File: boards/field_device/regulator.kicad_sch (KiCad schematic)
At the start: 13 parts, among them U5 HX8001-AJC

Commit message: assigned better footprints
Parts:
- C10: footprint Capacitor_SMD:C_0201_0603Metric -> Capacitor_SMD:C_0805_2012Metric_Pad1.18x1.45mm_HandSolder
- C11, C13: footprint Sensor_Current:LEM_HX02-P -> Capacitor_SMD:C_0603_1608Metric_Pad1.08x0.95mm_HandSolder
- C12: footprint Sensor_Current:LEM_HX02-P -> Capacitor_SMD:C_0805_2012Metric_Pad1.18x1.45mm_HandSolder
- D4: footprint (none) -> LED_SMD:LED_0603_1608Metric_Pad1.05x0.95mm_HandSolder
- L1: footprint (none) -> UnEasy-LCSC:IND-SMD_L4.0-W4.0_B
- R15, R16, R19, R20: footprint (none) -> Capacitor_SMD:C_0603_1608Metric_Pad1.08x0.95mm_HandSolder
- R17, R18: footprint (none) -> Resistor_SMD:R_0402_1005Metric_Pad0.72x0.64mm_HandSolder
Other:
- moved on the sheet: C10
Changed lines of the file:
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@@
-	)
-	(junction
-		(at 22.86 57.15)
-		(diameter 0)
-		(color 0 0 0 0)
 	)
 	(junction
@@
 		(color 0 0 0 0)
 	)
+	(junction
+		(at 19.05 36.83)
+		(diameter 0)
+		(color 0 0 0 0)
+	)
 	(no_connect
 		(at 100.33 34.29)
@@
 	(wire
 		(pts
-			(xy 62.23 50.8) (xy 62.23 52.07)
+			(xy 19.05 36.83) (xy 22.86 36.83)
 		)
 		(stroke
@@
 	(wire
 		(pts
-			(xy 64.77 31.75) (xy 64.77 34.29)
+			(xy 62.23 50.8) (xy 62.23 52.07)
 		)
 		(stroke
@@
 	(wire
 		(pts
-			(xy 64.77 34.29) (xy 80.01 34.29)
+			(xy 64.77 31.75) (xy 64.77 34.29)
 		)
 		(stroke
@@
 	(wire
 		(pts
-			(xy 62.23 49.53) (xy 62.23 50.8)
+			(xy 64.77 34.29) (xy 80.01 34.29)
 		)
 		(stroke
@@
 	(wire
 		(pts
-			(xy 21.59 57.15) (xy 22.86 57.15)
+			(xy 62.23 49.53) (xy 62.23 50.8)
 		)
 		(stroke
@@
 	(wire
 		(pts
-			(xy 100.33 31.75) (xy 115.57 31.75)
+			(xy 17.78 36.83) (xy 19.05 36.83)
 		)
 		(stroke
@@
 	(wire
 		(pts
-			(xy 35.56 36.83) (xy 80.01 36.83)
+			(xy 100.33 31.75) (xy 115.57 31.75)
 		)
 		(stroke
@@
 	(wire
 		(pts
-			(xy 107.95 39.37) (xy 107.95 36.83)
+			(xy 35.56 36.83) (xy 80.01 36.83)
 		)
 		(stroke
@@
 	(wire
 		(pts
-			(xy 64.77 50.8) (xy 64.77 34.29)
+			(xy 107.95 39.37) (xy 107.95 36.83)
 		)
 		(stroke
@@
 	(wire
 		(pts
-			(xy 34.29 36.83) (xy 35.56 36.83)
+			(xy 64.77 50.8) (xy 64.77 34.29)
 		)
 		(stroke
@@
 	(wire
 		(pts
-			(xy 22.86 36.83) (xy 26.67 36.83)
+			(xy 34.29 36.83) (xy 35.56 36.83)
 		)
 		(stroke
@@
 	(wire
 		(pts
-			(xy 50.8 41.91) (xy 62.23 41.91)
+			(xy 22.86 36.83) (xy 26.67 36.83)
 		)
 		(stroke
@@
 	(wire
 		(pts
-			(xy 22.86 36.83) (xy 22.86 57.15)
+			(xy 50.8 41.91) (xy 62.23 41.91)
 		)
 		(stroke
@@
 	(hierarchical_label "Vin"
 		(shape input)
-		(at 21.59 57.15 180)
+		(at 17.78 36.83 180)
 		(effects
 			(font
@@
 			)
 		)
-		(property "Footprint" ""
+		(property "Footprint" "Capacitor_SMD:C_0603_1608Metric_Pad1.08x0.95mm_HandSolder"
 			(at 113.792 35.56 90)
 			(hide yes)
@@
 			)
 		)
-		(property "Footprint" ""
+		(property "Footprint" "Capacitor_SMD:C_0603_1608Metric_Pad1.08x0.95mm_HandSolder"
 			(at 30.48 38.608 90)
 			(hide yes)
@@
 			)
 		)
-		(property "Footprint" ""
+		(property "Footprint" "Capacitor_SMD:C_0603_1608Metric_Pad1.08x0.95mm_HandSolder"
 			(at 68.58 33.528 90)
 			(hide yes)
@@
 		(dnp no)
 		(fields_autoplaced yes)
-		(property "Reference" "#PWR026"
+		(property "Reference" "#PWR027"
 			(at 22.86 40.64 0)
 			(hide yes)
@@
 			(project "field_device"
 				(path "/99623870-118f-49fe-bbf0-fb0b890db442/e9c11804-cc5e-4b00-a5de-7502c32ebb51/ed5659f9-5584-4daa-a017-4d4def535a07"
-					(reference "#PWR026")
+					(reference "#PWR027")
 					(unit 1)
 				)
@@
 			)
 		)
-		(property "Footprint" ""
+		(property "Footprint" "Capacitor_SMD:C_0603_1608Metric_Pad1.08x0.95mm_HandSolder"
 			(at 52.578 45.72 90)
 			(hide yes)
@@
 			)
 		)
-		(property "Footprint" ""
+		(property "Footprint" "Resistor_SMD:R_0402_1005Metric_Pad0.72x0.64mm_HandSolder"
 			(at 64.008 55.88 90)
 			(hide yes)
@@
 			)
 		)
-		(property "Footprint" ""
+		(property "Footprint" "UnEasy-LCSC:IND-SMD_L4.0-W4.0_B"
 			(at 104.14 36.83 0)
 			(hide yes)
@@
 			)
 		)
-		(property "Footprint" ""
+		(property "Footprint" "LED_SMD:LED_0603_1608Metric_Pad1.05x0.95mm_HandSolder"
 			(at 50.8 53.34 0)
 			(hide yes)
@@
 			)
 		)
-		(property "Footprint" "Sensor_Current:LEM_HX02-P"
+		(property "Footprint" "Capacitor_SMD:C_0603_1608Metric_Pad1.08x0.95mm_HandSolder"
 			(at 80.01 30.7848 0)
 			(hide yes)
@@
 			)
 		)
-		(property "Footprint" "Sensor_Current:LEM_HX02-P"
+		(property "Footprint" "Capacitor_SMD:C_0805_2012Metric_Pad1.18x1.45mm_HandSolder"
 			(at 73.9648 49.53 0)
 			(hide yes)
@@
 			)
 		)
-		(property "Footprint" "Sensor_Current:LEM_HX02-P"
+		(property "Footprint" "Capacitor_SMD:C_0603_1608Metric_Pad1.08x0.95mm_HandSolder"
 			(at 34.5948 44.45 0)
 			(hide yes)
@@
 			)
 		)
-		(property "Footprint" ""
+		(property "Footprint" "Resistor_SMD:R_0402_1005Metric_Pad0.72x0.64mm_HandSolder"
 			(at 64.008 45.72 90)
 			(hide yes)
@@
 	(symbol
 		(lib_id "power:GND")
-		(at 22.86 64.77 0)
+		(at 19.05 44.45 0)
 		(unit 1)
 		(body_style 1)
@@
 		(dnp no)
 		(fields_autoplaced yes)
-		(property "Reference" "#PWR027"
-			(at 22.86 71.12 0)
+		(property "Reference" "#PWR026"
+			(at 19.05 50.8 0)
 			(hide yes)
 			(show_name no)
@@
 		)
 		(property "Value" "GND"
-			(at 22.86 69.85 0)
+			(at 19.05 49.53 0)
 			(show_name no)
 			(do_not_autoplace no)
@@
 		)
 		(property "Footprint" ""
-			(at 22.86 64.77 0)
-			(hide yes)
-			(show_name no)
-			(do_not_autoplace no)
-			(effects
-				(font
-					(size 1.27 1.27)
-				)
-			)
-		)
-		(property "Datasheet" ""
-			(at 22.86 64.77 0)
+			(at 19.05 44.45 0)
+			(hide yes)
+			(show_name no)
+			(do_not_autoplace no)
+			(effects
+				(font
+					(size 1.27 1.27)
+				)
+			)
+		)
+		(property "Datasheet" ""
+			(at 19.05 44.45 0)
 			(hide yes)
 			(show_name no)
@@
 		)
 		(property "Description" "Power symbol creates a global label with name \"GND\" , ground"
-			(at 22.86 64.77 0)
-			(hide yes)
-			(show_name no)
-			(do_not_autoplace no)
-			(effects
-				(font
-					(size 1.27 1.27)
-				)
-			)
-		)
-		(pin "1"
-		)
-		(instances
-			(project "field_device"
-				(path "/99623870-118f-49fe-bbf0-fb0b890db442/e9c11804-cc5e-4b00-a5de-7502c32ebb51/ed5659f9-5584-4daa-a017-4d4def535a07"
-					(reference "#PWR027")
+			(at 19.05 44.45 0)
+			(hide yes)
+			(show_name no)
+			(do_not_autoplace no)
+			(effects
+				(font
+					(size 1.27 1.27)
+				)
+			)
+		)
+		(pin "1"
+		)
+		(instances
+			(project "field_device"
+				(path "/99623870-118f-49fe-bbf0-fb0b890db442/e9c11804-cc5e-4b00-a5de-7502c32ebb51/ed5659f9-5584-4daa-a017-4d4def535a07"
+					(reference "#PWR026")
 					(unit 1)
 				)
@@
 	(symbol
 		(lib_id "Device:C")
-		(at 22.86 60.96 0)
+		(at 19.05 40.64 0)
 		(unit 1)
 		(body_style 1)
@@
 		(fields_autoplaced yes)
 		(property "Reference" "C10"
-			(at 26.67 59.6899 0)
+			(at 22.86 39.3699 0)
 			(show_name no)
 			(do_not_autoplace no)
@@
 		)
 		(property "Value" "10u"
-			(at 26.67 62.2299 0)
+			(at 22.86 41.9099 0)
 			(show_name no)
 			(do_not_autoplace no)
@@
 			)
 		)
-		(property "Footprint" "Capacitor_SMD:C_0201_0603Metric"
-			(at 23.8252 64.77 0)
-			(hide yes)
-			(show_name no)
-			(do_not_autoplace no)
-			(effects
-				(font
-					(size 1.27 1.27)
-				)
-			)
-		)
-		(property "Datasheet" ""
-			(at 22.86 60.96 0)
+		(property "Footprint" "Capacitor_SMD:C_0805_2012Metric_Pad1.18x1.45mm_HandSolder"
+			(at 20.0152 44.45 0)
+			(hide yes)
+			(show_name no)
+			(do_not_autoplace no)
+			(effects
+				(font
+					(size 1.27 1.27)
+				)
+			)
+		)
+		(property "Datasheet" ""
+			(at 19.05 40.64 0)
 			(hide yes)
 			(show_name no)
@@
 		)
 		(property "Description" "Unpolarized capacitor"
-			(at 22.86 60.96 0)
-			(hide yes)
-			(show_name no)
+			(at 19.05 40.64 0)
+			(hide yes)
+			(show_name no)

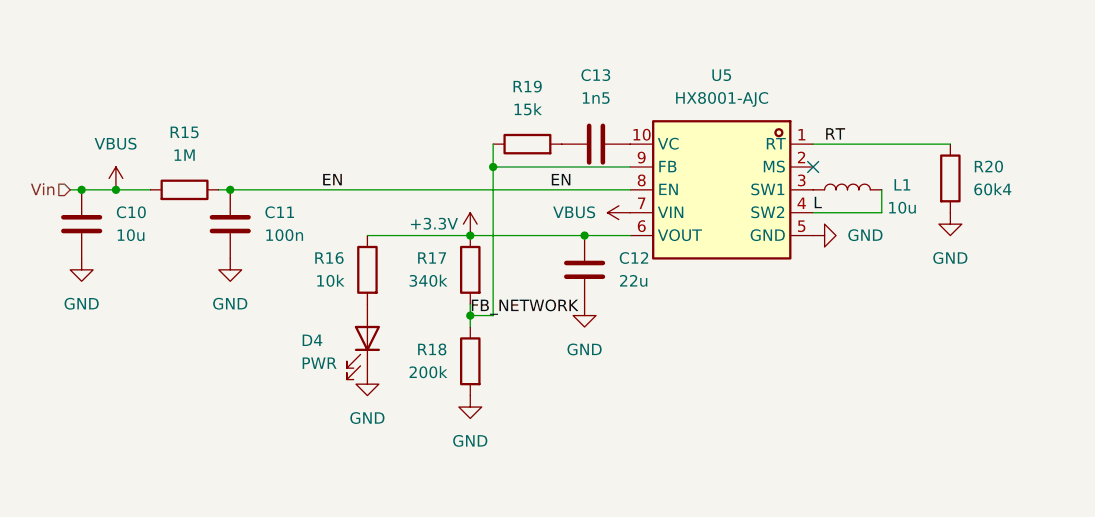
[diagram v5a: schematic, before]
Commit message: changed regulator
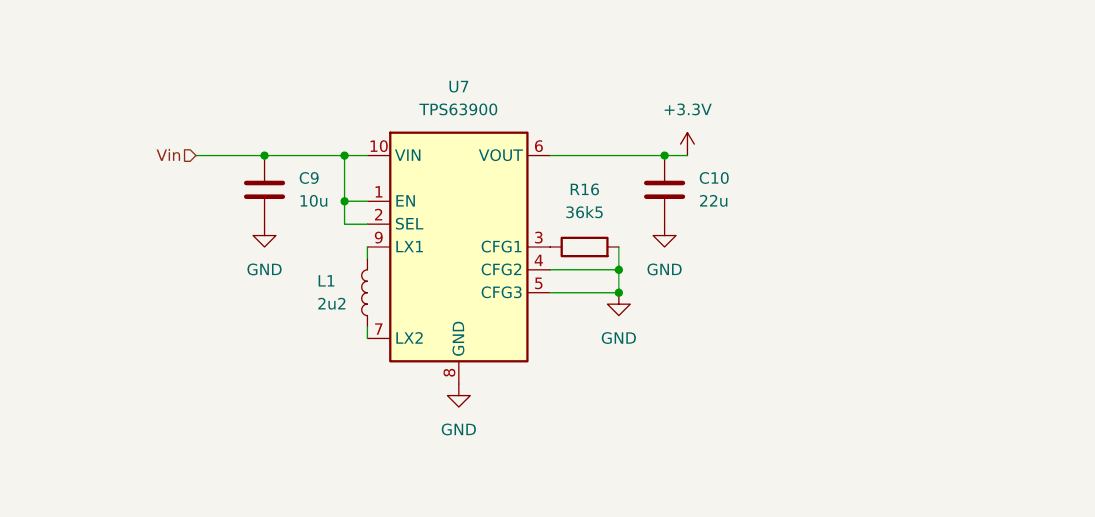
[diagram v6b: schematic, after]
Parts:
- removed C11: 100n, Capacitor_SMD:C_0603_1608Metric_Pad1.08x0.95mm_HandSolder, symbol Device:C
- removed C12: 22u, Capacitor_SMD:C_0805_2012Metric_Pad1.18x1.45mm_HandSolder, symbol Device:C
- removed C13: 1n5, Capacitor_SMD:C_0603_1608Metric_Pad1.08x0.95mm_HandSolder, symbol Device:C
- removed D4: PWR, LED_SMD:LED_0603_1608Metric_Pad1.05x0.95mm_HandSolder, symbol Device:LED
- removed R15: 1M, Capacitor_SMD:C_0603_1608Metric_Pad1.08x0.95mm_HandSolder, symbol Device:R
- removed R17: 340k, Resistor_SMD:R_0402_1005Metric_Pad0.72x0.64mm_HandSolder, symbol Device:R
- removed R18: 200k, Resistor_SMD:R_0402_1005Metric_Pad0.72x0.64mm_HandSolder, symbol Device:R
- removed R19: 15k, Capacitor_SMD:C_0603_1608Metric_Pad1.08x0.95mm_HandSolder, symbol Device:R
- removed R20: 60k4, Capacitor_SMD:C_0603_1608Metric_Pad1.08x0.95mm_HandSolder, symbol Device:R
- removed U5: HX8001-AJC, LCSC downloads:MSOP-10_L3.0-W3.0-P0.50-LS5.0-BL, symbol lcsc downloads:HX8001-AJC
- added C9: 10u, Capacitor_SMD:C_0603_1608Metric_Pad1.08x0.95mm_HandSolder, symbol Device:C
- added U7: TPS63900, Package_SON:WSON-10-1EP_2.5x2.5mm_P0.5mm_EP1.2x2mm_ThermalVias, symbol Regulator_Switching:TPS63900
- C10: value 10u -> 22u; footprint Capacitor_SMD:C_0805_2012Metric_Pad1.18x1.45mm_HandSolder -> Capacitor_SMD:C_0603_1608Metric_Pad1.08x0.95mm_HandSolder
- L1: value 10u -> 2u2; footprint UnEasy-LCSC:IND-SMD_L4.0-W4.0_B -> (none)
- R16: value 10k -> 36k5; footprint Capacitor_SMD:C_0603_1608Metric_Pad1.08x0.95mm_HandSolder -> Resistor_SMD:R_0402_1005Metric_Pad0.72x0.64mm_HandSolder
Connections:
- net VBUS is gone; now on net +3.3V: C10.1
- net +3.3V: now also U7.6 (VOUT); no longer R16.1
- net GND: now also R16.2, C9.2, U7.11 (GND), U7.4 (CFG2), U7.5 (CFG3), U7.8 (GND)
- net at L1.1: now also U7.7 (LX2)
- net L: no longer names the net of L1.2
- net L: now also U7.9 (LX1)
- new net: R16.1, U7.3 (CFG1)
- new net Vin: C9.1, U7.1 (EN), U7.10 (VIN), U7.2 (SEL)
- no-connect marks 1 -> 0

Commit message: added inductor footprint and did regulator routing
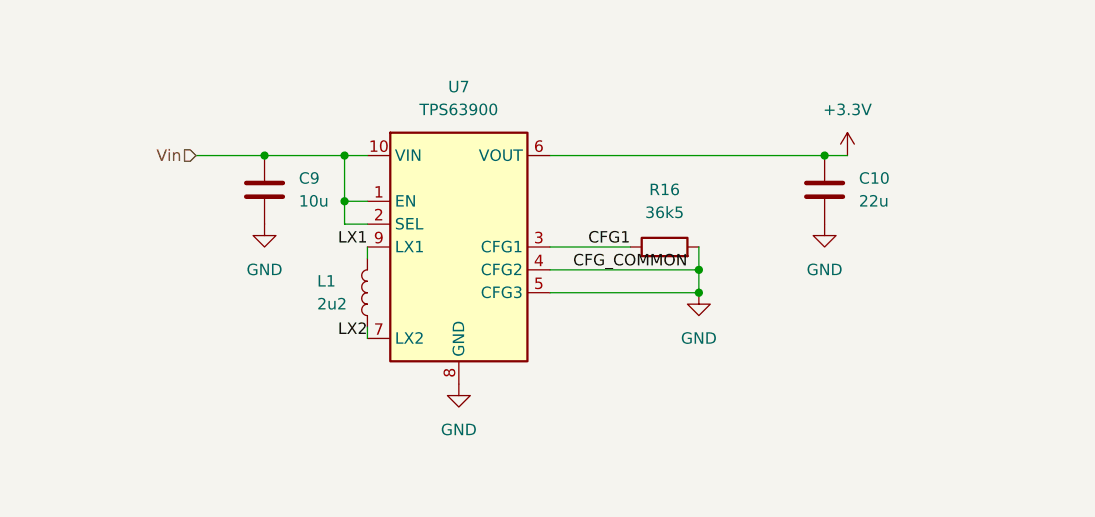
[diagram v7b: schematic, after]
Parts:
- L1: footprint (none) -> UnEasy-LCSC:IND-SMD_L4.0-W4.0_B
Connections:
- net CFG1: now reaches R16.1, U7.3 (CFG1)
- net LX2: now reaches L1.1, U7.7 (LX2)
- net LX1: now reaches L1.2, U7.9 (LX1)
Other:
- moved on the sheet: C10, R16
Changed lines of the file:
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@@
 	(paper "A4")
 	(junction
-		(at 83.82 33.02)
+		(at 101.6 33.02)
 		(diameter 0)
 		(color 0 0 0 0)
 	)
 	(junction
-		(at 78.74 45.72)
+		(at 87.63 45.72)
 		(diameter 0)
 		(color 0 0 0 0)
@@
 	)
 	(junction
-		(at 78.74 48.26)
+		(at 87.63 48.26)
 		(diameter 0)
 		(color 0 0 0 0)
@@
 	(wire
 		(pts
-			(xy 78.74 45.72) (xy 78.74 43.18)
+			(xy 71.12 48.26) (xy 87.63 48.26)
+		)
+		(stroke
+			(width 0)
+			(type default)
+		)
+	)
+	(wire
+		(pts
+			(xy 71.12 45.72) (xy 87.63 45.72)
+		)
+		(stroke
+			(width 0)
+			(type default)
+		)
+	)
+	(wire
+		(pts
+			(xy 87.63 45.72) (xy 87.63 43.18)
 		)
 		(stroke
@@
 	(wire
 		(pts
+			(xy 80.01 43.18) (xy 71.12 43.18)
+		)
+		(stroke
+			(width 0)
+			(type default)
+		)
+	)
+	(wire
+		(pts
 			(xy 48.26 40.64) (xy 50.8 40.64)
 		)
@@
 	(wire
 		(pts
-			(xy 71.12 33.02) (xy 86.36 33.02)
+			(xy 71.12 33.02) (xy 104.14 33.02)
 		)
 		(stroke
@@
 	(wire
 		(pts
-			(xy 78.74 48.26) (xy 78.74 45.72)
-		)
-		(stroke
-			(width 0)
-			(type default)
-		)
-	)
-	(wire
-		(pts
-			(xy 71.12 48.26) (xy 78.74 48.26)
+			(xy 87.63 48.26) (xy 87.63 45.72)
 		)
 		(stroke
@@
 		)
 	)
-	(wire
-		(pts
-			(xy 71.12 45.72) (xy 78.74 45.72)
-		)
-		(stroke
-			(width 0)
-			(type default)
+	(label "LX1"
+		(at 50.8 43.18 180)
+		(effects
+			(font
+				(size 1.27 1.27)
+			)
+			(justify right bottom)
+		)
+	)
+	(label "CFG_COMMON"
+		(at 86.36 45.72 180)
+		(effects
+			(font
+				(size 1.27 1.27)
+			)
+			(justify right bottom)
+		)
+	)
+	(label "CFG1"
+		(at 80.01 43.18 180)
+		(effects
+			(font
+				(size 1.27 1.27)
+			)
+			(justify right bottom)
+		)
+	)
+	(label "LX2"
+		(at 50.8 53.34 180)
+		(effects
+			(font
+				(size 1.27 1.27)
+			)
+			(justify right bottom)
 		)
 	)
@@
 	(symbol
 		(lib_id "power:GND")
-		(at 78.74 48.26 0)
+		(at 87.63 48.26 0)
 		(unit 1)
 		(body_style 1)
@@
 		(fields_autoplaced yes)
 		(property "Reference" "#PWR030"
-			(at 78.74 54.61 0)
+			(at 87.63 54.61 0)
 			(hide yes)
 			(show_name no)
@@
 		)
 		(property "Value" "GND"
-			(at 78.74 53.34 0)
+			(at 87.63 53.34 0)
 			(show_name no)
 			(do_not_autoplace no)
@@
 		)
 		(property "Footprint" ""
-			(at 78.74 48.26 0)
+			(at 87.63 48.26 0)
 			(hide yes)
 			(show_name no)
@@
 		)
 		(property "Datasheet" ""
-			(at 78.74 48.26 0)
+			(at 87.63 48.26 0)
 			(hide yes)
 			(show_name no)
@@
 		)
 		(property "Description" "Power symbol creates a global label with name \"GND\" , ground"
-			(at 78.74 48.26 0)
+			(at 87.63 48.26 0)
 			(hide yes)
 			(show_name no)
@@
 	(symbol
 		(lib_id "Device:C")
-		(at 83.82 36.83 0)
+		(at 101.6 36.83 0)
 		(unit 1)
 		(body_style 1)
@@
 		(fields_autoplaced yes)
 		(property "Reference" "C10"
-			(at 87.63 35.5599 0)
+			(at 105.41 35.5599 0)
 			(show_name no)
 			(do_not_autoplace no)
@@
 		)
 		(property "Value" "22u"
-			(at 87.63 38.0999 0)
+			(at 105.41 38.0999 0)
 			(show_name no)
 			(do_not_autoplace no)
@@
 		)
 		(property "Footprint" "Capacitor_SMD:C_0603_1608Metric_Pad1.08x0.95mm_HandSolder"
-			(at 84.7852 40.64 0)
+			(at 102.5652 40.64 0)
 			(hide yes)
 			(show_name no)
@@
 		)
 		(property "Datasheet" ""
-			(at 83.82 36.83 0)
+			(at 101.6 36.83 0)
 			(hide yes)
 			(show_name no)
@@
 		)
 		(property "Description" "Unpolarized capacitor"
-			(at 83.82 36.83 0)
+			(at 101.6 36.83 0)
 			(hide yes)
 			(show_name no)
@@
 	(symbol
 		(lib_id "power:+3.3V")
-		(at 86.36 33.02 0)
+		(at 104.14 33.02 0)
 		(unit 1)
 		(body_style 1)
@@
 		(fields_autoplaced yes)
 		(property "Reference" "#PWR029"
-			(at 86.36 36.83 0)
+			(at 104.14 36.83 0)
 			(hide yes)
 			(show_name no)
@@
 		)
 		(property "Value" "+3.3V"
-			(at 86.36 27.94 0)
+			(at 104.14 27.94 0)
 			(show_name no)
 			(do_not_autoplace no)
@@
 		)
 		(property "Footprint" ""
-			(at 86.36 33.02 0)
+			(at 104.14 33.02 0)
 			(hide yes)
 			(show_name no)
@@
 		)
 		(property "Datasheet" ""
-			(at 86.36 33.02 0)
+			(at 104.14 33.02 0)
 			(hide yes)
 			(show_name no)
@@
 		)
 		(property "Description" "Power symbol creates a global label with name \"+3.3V\""
-			(at 86.36 33.02 0)
+			(at 104.14 33.02 0)
 			(hide yes)
 			(show_name no)
@@
 			)
 		)
-		(property "Footprint" ""
+		(property "Footprint" "UnEasy-LCSC:IND-SMD_L4.0-W4.0_B"
 			(at 50.8 48.26 0)
 			(hide yes)
@@
 	(symbol
 		(lib_id "power:GND")
-		(at 83.82 40.64 0)
+		(at 101.6 40.64 0)
 		(unit 1)
 		(body_style 1)
@@
 		(fields_autoplaced yes)
 		(property "Reference" "#PWR028"
-			(at 83.82 46.99 0)
+			(at 101.6 46.99 0)
 			(hide yes)
 			(show_name no)
@@
 		)
 		(property "Value" "GND"
-			(at 83.82 45.72 0)
+			(at 101.6 45.72 0)
 			(show_name no)
 			(do_not_autoplace no)
@@
 		)
 		(property "Footprint" ""
-			(at 83.82 40.64 0)
+			(at 101.6 40.64 0)
 			(hide yes)
 			(show_name no)
@@
 		)
 		(property "Datasheet" ""
-			(at 83.82 40.64 0)
+			(at 101.6 40.64 0)
 			(hide yes)
 			(show_name no)
@@
 		)
 		(property "Description" "Power symbol creates a global label with name \"GND\" , ground"
-			(at 83.82 40.64 0)
+			(at 101.6 40.64 0)
 			(hide yes)
 			(show_name no)
@@
 	(symbol
 		(lib_id "Device:R")
-		(at 74.93 43.18 90)
+		(at 83.82 43.18 90)
 		(unit 1)
 		(body_style 1)
@@
 		(fields_autoplaced yes)
 		(property "Reference" "R16"
-			(at 74.93 36.83 90)
+			(at 83.82 36.83 90)
 			(show_name no)
 			(do_not_autoplace no)
@@
 		)
 		(property "Value" "36k5"
-			(at 74.93 39.37 90)
+			(at 83.82 39.37 90)
 			(show_name no)
 			(do_not_autoplace no)
@@
 		)
 		(property "Footprint" "Resistor_SMD:R_0402_1005Metric_Pad0.72x0.64mm_HandSolder"
-			(at 74.93 44.958 90)
+			(at 83.82 44.958 90)
 			(hide yes)
 			(show_name no)
@@
 		)
 		(property "Datasheet" ""
-			(at 74.93 43.18 0)
+			(at 83.82 43.18 0)
 			(hide yes)
 			(show_name no)
@@
 		)
 		(property "Description" "Resistor"
-			(at 74.93 43.18 0)
-			(hide yes)
-			(show_name no)
+			(at 83.82 43.18 0)
+			(hide yes)
+			(show_name no)

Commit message: refined schematic
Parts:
- renumbered U7 to U5
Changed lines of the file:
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@@
 		(dnp no)
 		(fields_autoplaced yes)
-		(property "Reference" "U7"
+		(property "Reference" "U5"
 			(at 60.96 25.4 0)
 			(show_name no)
@@
 			(project "field_device"
 				(path "/99623870-118f-49fe-bbf0-fb0b890db442/e9c11804-cc5e-4b00-a5de-7502c32ebb51/ed5659f9-5584-4daa-a017-4d4def535a07"
-					(reference "U7")
+					(reference "U5")
 					(unit 1)
 				)
@@
 		(dnp no)
 		(fields_autoplaced yes)
-		(property "Reference" "#PWR029"
+		(property "Reference" "#PWR032"
 			(at 104.14 36.83 0)
 			(hide yes)
@@
 			(project "field_device"
 				(path "/99623870-118f-49fe-bbf0-fb0b890db442/e9c11804-cc5e-4b00-a5de-7502c32ebb51/ed5659f9-5584-4daa-a017-4d4def535a07"
-					(reference "#PWR029")
+					(reference "#PWR032")
 					(unit 1)
 				)
@@
 		(dnp no)
 		(fields_autoplaced yes)
-		(property "Reference" "#PWR028"
+		(property "Reference" "#PWR031"
 			(at 101.6 46.99 0)
 			(hide yes)
@@
 			(project "field_device"
 				(path "/99623870-118f-49fe-bbf0-fb0b890db442/e9c11804-cc5e-4b00-a5de-7502c32ebb51/ed5659f9-5584-4daa-a017-4d4def535a07"
-					(reference "#PWR028")
+					(reference "#PWR031")
 					(unit 1)
 				)
@@
 		(dnp no)
 		(fields_autoplaced yes)
-		(property "Reference" "#PWR026"
+		(property "Reference" "#PWR028"
 			(at 39.37 46.99 0)
 			(hide yes)
@@
 			(project "field_device"
 				(path "/99623870-118f-49fe-bbf0-fb0b890db442/e9c11804-cc5e-4b00-a5de-7502c32ebb51/ed5659f9-5584-4daa-a017-4d4def535a07"
-					(reference "#PWR026")
+					(reference "#PWR028")
 					(unit 1)
 				)
@@
 		(dnp no)
 		(fields_autoplaced yes)
-		(property "Reference" "#PWR027"
+		(property "Reference" "#PWR029"
 			(at 60.96 64.77 0)
 			(hide yes)
@@
 			(project "field_device"
 				(path "/99623870-118f-49fe-bbf0-fb0b890db442/e9c11804-cc5e-4b00-a5de-7502c32ebb51/ed5659f9-5584-4daa-a017-4d4def535a07"
-					(reference "#PWR027")
-					(unit 1)
-				)
+					(reference "#PWR029")
+					(unit 1)
+				)
